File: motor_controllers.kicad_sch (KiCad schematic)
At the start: 23 parts, among them IC3 L6470HTR, IC4 L6470HTR, IC6 74AUP2G00DC,125

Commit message: New complete schematic version
May need to resize the resistors, also need to change the caps back to electrolytic
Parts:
- removed C47: 100nF, symbol Device:C
- removed R41: 10k, symbol Device:R
- removed R42: 27k, symbol Device:R
- added C24, C25, C30, C31: 47uF, parts:CAPAE660X850N, symbol Device:C_Polarized
- added C32: 100nF, Capacitor_SMD:C_0603_1608Metric, symbol Device:C
- added R22: 10k, Resistor_SMD:R_0603_1608Metric, symbol Device:R
- added R23: 27k, Resistor_SMD:R_0603_1608Metric, symbol Device:R
- C22: renamed from C41; footprint (none) -> Capacitor_SMD:C_0805_2012Metric
- C23: renamed from C42; footprint (none) -> Capacitor_SMD:C_0603_1608Metric
- C26: renamed from C43; footprint (none) -> Capacitor_SMD:C_0603_1608Metric
- C27: renamed from C44; footprint (none) -> Capacitor_SMD:C_0603_1608Metric
- C28: renamed from C45; footprint (none) -> Capacitor_SMD:C_0805_2012Metric
- C29: renamed from C46; footprint (none) -> Capacitor_SMD:C_0603_1608Metric
- C33: renamed from C48; footprint (none) -> Capacitor_SMD:C_0603_1608Metric
- C34: renamed from C49; footprint (none) -> Capacitor_SMD:C_0603_1608Metric
- IC5: renamed from IC6; footprint SOP50P310X100-8N -> parts:SOP50P310X100-8N
- R20: renamed from R39; footprint (none) -> Resistor_SMD:R_0603_1608Metric
- R21: renamed from R40; footprint (none) -> Resistor_SMD:R_0603_1608Metric
- R34, R35, R36, R37, R38: footprint (none) -> Resistor_SMD:R_0603_1608Metric
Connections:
- net +24V: now also C26.2, R20.2, C24.1, C25.1, C30.1, C31.1, C32.2, R22.2
- net MR_ADCIN: now also R22.1, R23.2
- net at C26.1, R21.1: now also C24.2, C25.2
- net BUSY renamed M_BUSY
- net FLAG renamed M_FLAG
- net ~{SPI_CS} renamed ~{SPI_CS_M}
- net ~{STBY} renamed ~{M_STBY}
- new net: C30.2, C31.2, C32.1, R23.1
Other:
- note added: "Point in circle should be connected to analog ground!"
- moved on the sheet: R20, R21

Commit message: Uploaded all project files, finished PCB design
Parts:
- removed C24, C25, C30, C31: 47uF, parts:CAPAE660X850N, symbol Device:C_Polarized
- added C31, C37: 220nF, Capacitor_SMD:C_0805_2012Metric, symbol Device:C
- added C33, C39: 100uF, parts:CAPAE1030X1100N, symbol Device:C_Polarized
- C34: renamed from C26; value 100nF -> 220nF; footprint Capacitor_SMD:C_0603_1608Metric -> Capacitor_SMD:C_0805_2012Metric
- C40: renamed from C32; value 100nF -> 220nF; footprint Capacitor_SMD:C_0603_1608Metric -> Capacitor_SMD:C_0805_2012Metric
- D1, D2: footprint parts:ZXMP6A13FTA -> parts:BAV99215
- IC3, IC4: value L6470HTR -> L6470H
- R19: renamed from R20; value 10k -> 27k
- R20: renamed from R21; value 27k -> 10k
- R21: renamed from R22; value 10k -> 27k
- R22: renamed from R23; value 27k -> 10k
- renumbered C22 to C30, C23 to C32, C27 to C35, C28 to C36, C29 to C38, C33 to C41, C34 to C42
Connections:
- net +24V: now also C31.2, C33.1, C37.2, C39.1
- net GND: now also C34.1, C40.1, R20.1, R22.1, C33.2, C39.2
- net ML_VBOOT: now also C31.1
- net MR_VBOOT: now also C37.1
- net CLK_SYNC: now reaches IC4.7 (OSCIN)
- net CLK_SYNC: now also IC3.8 (OSCOUT)
- net OSCOUT: no longer names the net of IC4.8 (OSCOUT)
- net OSCOUT: no longer IC3.8 (OSCOUT)
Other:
- moved on the sheet: C30, C34, C36, C40, R19, R20, R21, R22

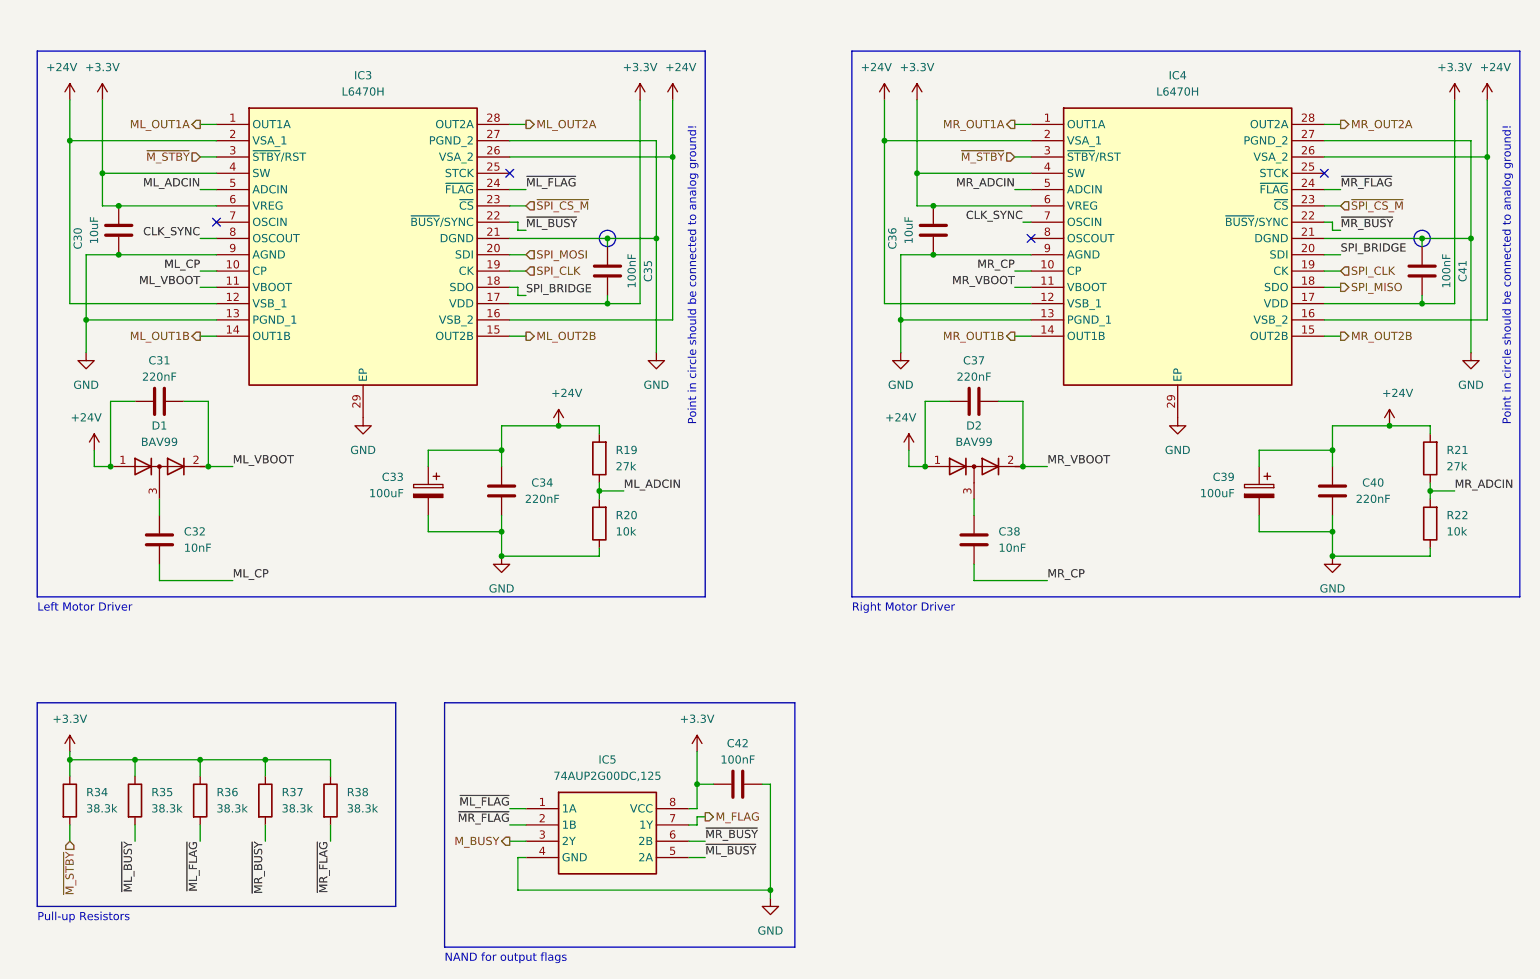
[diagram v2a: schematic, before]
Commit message: Added 3V0 net for L6470H's internal voltage regulator and updated schematic with stabilization caps
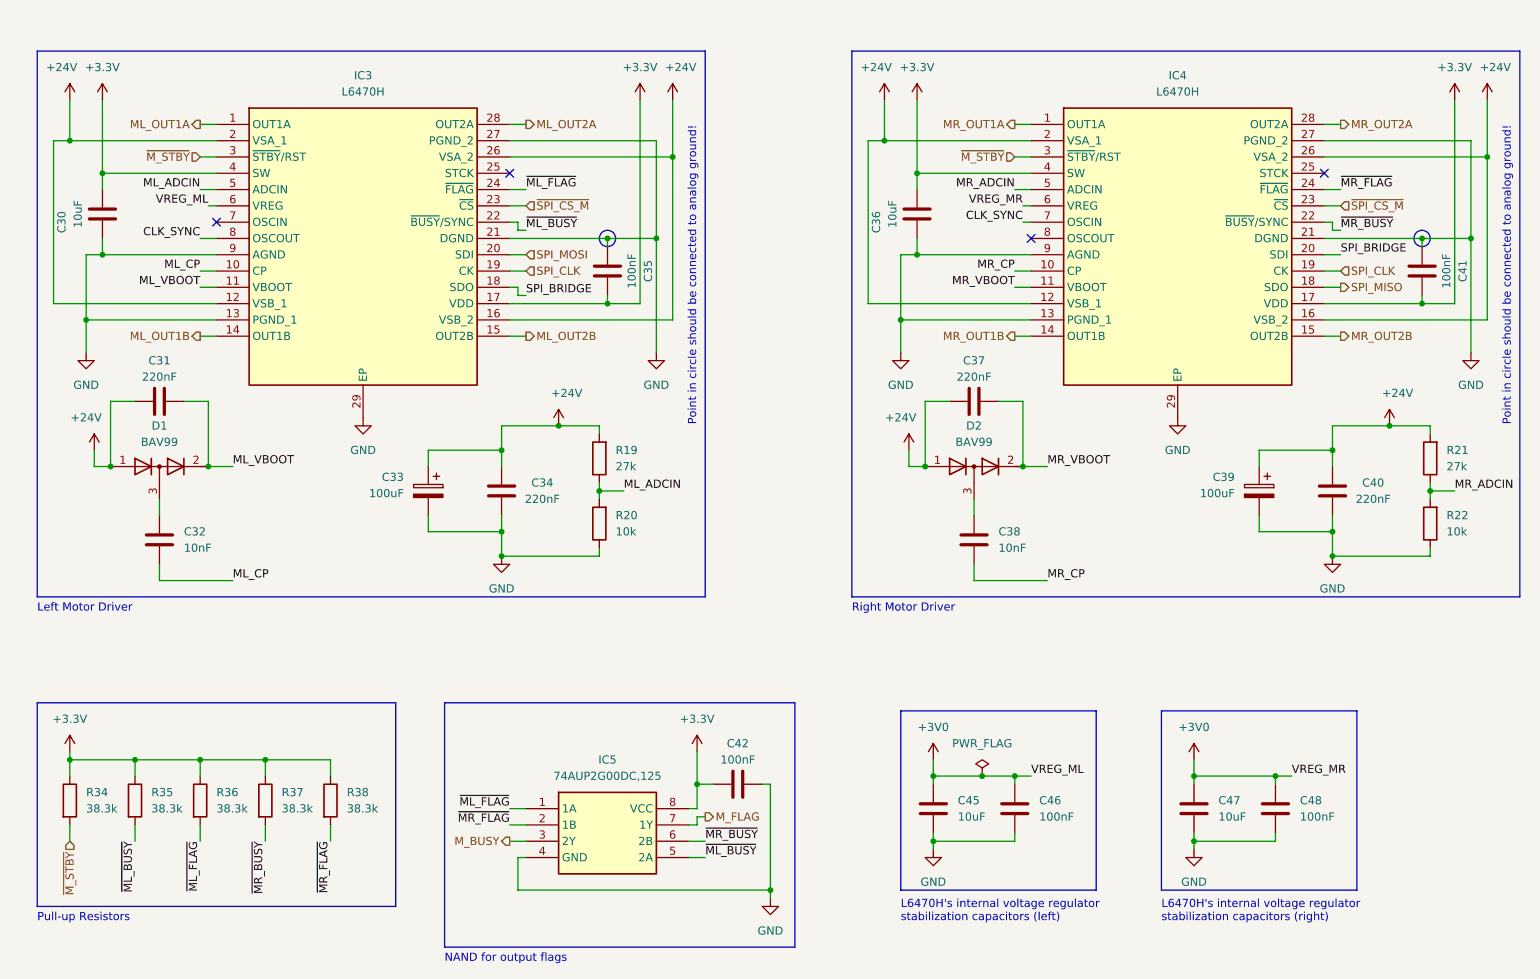
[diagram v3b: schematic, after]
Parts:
- added C45, C47: 10uF, Capacitor_SMD:C_0805_2012Metric, symbol Device:C
- added C46, C48: 100nF, Capacitor_SMD:C_0603_1608Metric, symbol Device:C
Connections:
- net +3.3V: no longer IC3.6 (VREG), IC4.6 (VREG)
- net GND: now also C45.2, C46.2, C47.2, C48.2
- new net +3V0: C45.1, C46.1, C47.1, C48.1, IC3.6 (VREG), IC4.6 (VREG)
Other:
- note added: "L6470H's internal voltage regulator stabilization capacitors (left)"
- note added: "L6470H's internal voltage regulator stabilization capacitors (right)"
- moved on the sheet: C30, C36

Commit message: Separated 3V0 and 3V3 lines, right motor driver properly connected, fixed trace pathing
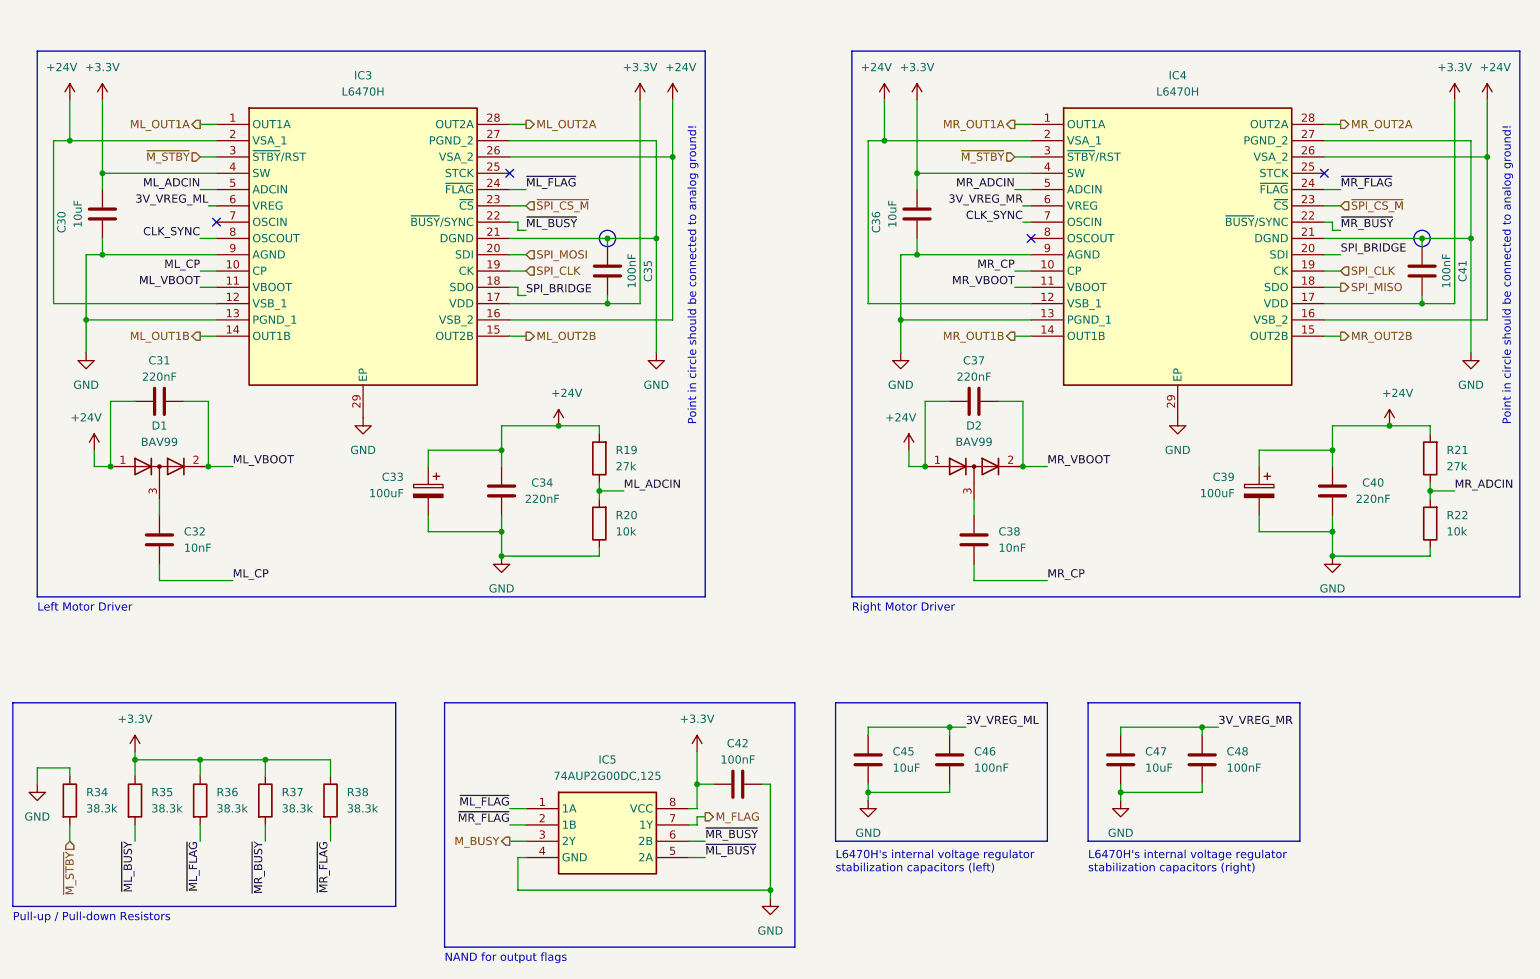
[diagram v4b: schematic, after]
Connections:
- net +3.3V: no longer R34.1
- net GND: now also R34.1
- net +3V0 renamed 3V_VREG_ML
- net 3V_VREG_ML: no longer C47.1, C48.1, IC4.6 (VREG)
- new net 3V_VREG_MR: C47.1, C48.1, IC4.6 (VREG)
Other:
- note added: "Pull-up / Pull-down Resistors"
- note removed: "Pull-up Resistors"
- moved on the sheet: C45, C46, C47, C48
